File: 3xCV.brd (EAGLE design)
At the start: 96.8 x 54 mm, 90 parts, among them IC1 TL074, IC2 TL074, IC3 TL074, SW1 TL2285

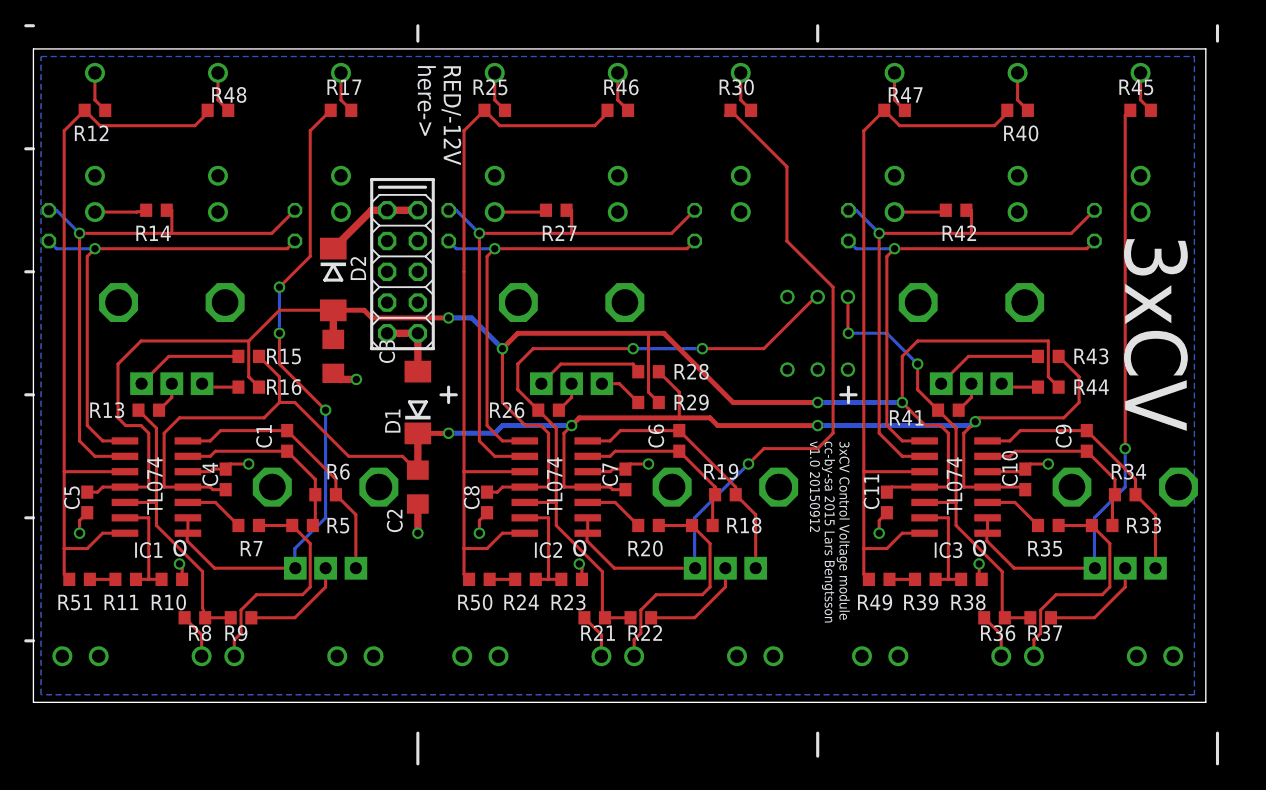
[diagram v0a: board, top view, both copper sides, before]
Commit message: Somewhat modified. No thru jacks (out of space). Aligned input jacks with outputs.
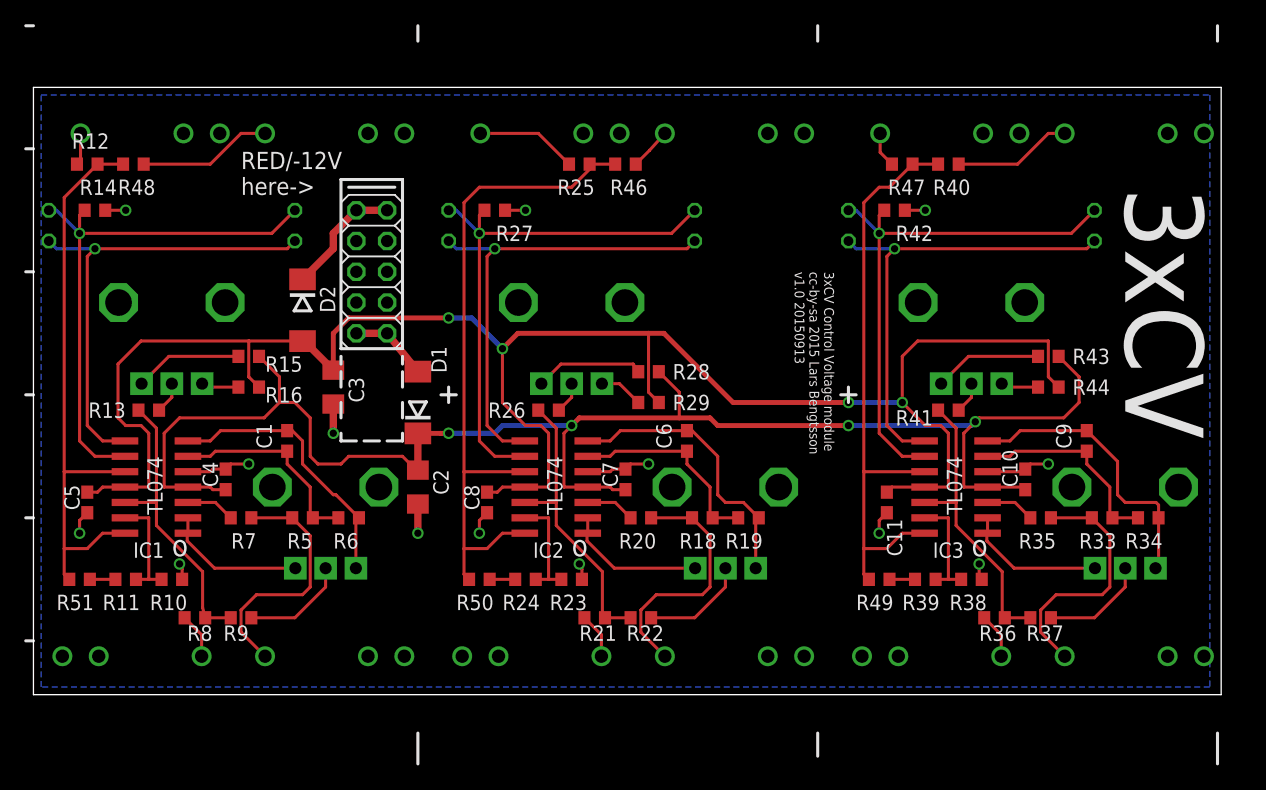
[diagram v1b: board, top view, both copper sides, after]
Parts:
- removed R17, R30, R45: 220, rcl:R0603
- removed SW1: TL2285, lb_devs:TL2285_PCB
- removed THRU, THRU1, THRU2: WQP-PJ301M-12_JACK, thonkiconn:WQP-PJ301M-12_JACK
- moved OUT2 8.89 mm to (91.4, 52.1), turned to 270 degrees
- moved OUT3 8.89 mm to (58.4, 52.1), turned to 270 degrees
- moved OUT5 8.89 mm to (25.4, 52.1), turned to 270 degrees
- moved R25 8.28 mm to (46.4, 49.5), turned to 180 degrees
- moved R48 8.28 mm to (9.53, 49.5)
- moved R40 7.24 mm to (76.8, 49.5)
- moved R27 5.08 mm to (39.4, 45.7), turned to 180 degrees
- moved R14 5.08 mm to (6.35, 45.7), turned to 180 degrees
- moved R42 5.08 mm to (72.4, 45.7), turned to 180 degrees
- moved R12 4.49 mm to (5.71, 49.5), turned to 180 degrees
- moved R47 4.49 mm to (73.0, 49.5), turned to 180 degrees
- moved R46 4.49 mm to (50.2, 49.5)
- moved OUT1 3.81 mm to (43.2, 52.1), turned to 270 degrees
- moved OUT4 3.81 mm to (76.2, 52.1), turned to 270 degrees
- moved OUT 3.81 mm to (10.2, 52.1), turned to 270 degrees
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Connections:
- removed net N$18: R17.2, THRU.P$1
- removed net N$38: R30.2, THRU1.P$1
- removed net N$55: R45.2, THRU2.P$1
- net GND: no longer THRU.P$3, THRU1.P$3, THRU2.P$3
- net MIX1: no longer SW1.3
- net MIX2: no longer SW1.2
- net N$25: no longer R30.1
- net N$42: no longer R45.1
- net N$5: no longer R17.1
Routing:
- net N$25: track 61.1 -> 11.8 mm, vias 1 -> 0
- net N$5: track 54.0 -> 11.8 mm, vias 3 -> 0
- net N$42: track 50.9 -> 11.8 mm, vias 1 -> 0
- net MIX2: track 55.7 -> 24.1 mm, vias 2 -> 0
- net MIX1: track 39.1 -> 24.8 mm, vias 2 -> 0
- net N$13: track 61.5 -> 48.3 mm
- net N$47: track 61.5 -> 49.3 mm
- net N$56: track 3.45 -> 11.1 mm
- net GND: track 43.5 -> 36.0 mm, vias 11 -> 14
- net N$49: track 3.45 -> 9.81 mm
- net N$57: track 61.5 -> 55.9 mm
- net N$32: track 3.45 -> 8.38 mm
- net N$55: track 3.45 -> 0.00 mm
- net N$38: track 3.45 -> 0.00 mm
- net N$18: track 3.45 -> 0.00 mm
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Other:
- board size 96.8 x 54 mm -> 98.1 x 50.2 mm
- board text added: "3xCV Control Voltage module cc-by-sa 2015 Lars Bengtsson v1.0 20150913"
- board text removed: "3xCV Control Voltage module cc-by-sa 2015 Lars Bengtsson v1.0 20150912"

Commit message: Added back 1+2 mix button. There is room for it. Yay! =)
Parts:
- added SW1: TL2285, lb_devs:TL2285_PCB
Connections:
- net MIX1: now also SW1.3
- net MIX2: now also SW1.2
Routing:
- net MIX1: track 24.8 -> 79.0 mm
- net MIX2: track 24.1 -> 73.9 mm
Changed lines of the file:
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@@
 <text x="45.72" y="17.145" size="1.778" layer="25" font="vector">o</text>
 <text x="78.74" y="17.145" size="1.778" layer="25" font="vector">o</text>
-<text x="64.135" y="40.64" size="0.8128" layer="25" font="vector" rot="SR270">3xCV Control Voltage module
+<text x="59.69" y="33.02" size="0.8128" layer="25" font="vector" rot="SR270">3xCV Control Voltage module
 cc-by-sa 2015 Lars Bengtsson
 v1.0 20150913</text>
@@
 <attribute name="VALUE" x="4.445" y="13.335" size="1.27" layer="27"/>
 </element>
+<element name="SW1" library="lb_devs" package="TL2285_PCB" value="TL2285" x="64.77" y="38.1" rot="MR0"/>
 </elements>
 <signals>
@@
 <wire x1="54.61" y1="28.575" x2="57.15" y2="28.575" width="0.4064" layer="1"/>
 <wire x1="57.15" y1="28.575" x2="57.785" y2="27.94" width="0.4064" layer="1"/>
-<wire x1="57.785" y1="27.94" x2="68.58" y2="27.94" width="0.4064" layer="1"/>
-<via x="68.58" y="27.94" extent="1-16" drill="0.6" shape="octagon"/>
-<wire x1="68.58" y1="27.94" x2="78.74" y2="27.94" width="0.4064" layer="16"/>
+<wire x1="57.785" y1="27.94" x2="66.04" y2="27.94" width="0.4064" layer="1"/>
+<via x="66.04" y="27.94" extent="1-16" drill="0.6" shape="octagon"/>
+<wire x1="66.04" y1="27.94" x2="78.74" y2="27.94" width="0.4064" layer="16"/>
 <wire x1="78.74" y1="27.94" x2="79.0575" y2="28.2575" width="0.4064" layer="16"/>
 <via x="79.0575" y="28.2575" extent="1-16" drill="0.6" shape="octagon"/>
@@
 <wire x1="52.07" y1="35.56" x2="53.34" y2="35.56" width="0.4064" layer="1"/>
 <wire x1="53.34" y1="35.56" x2="59.055" y2="29.845" width="0.4064" layer="1"/>
-<wire x1="59.055" y1="29.845" x2="68.58" y2="29.845" width="0.4064" layer="1"/>
-<via x="68.58" y="29.845" extent="1-16" drill="0.6" shape="octagon"/>
-<wire x1="68.58" y1="29.845" x2="73.025" y2="29.845" width="0.4064" layer="16"/>
+<wire x1="59.055" y1="29.845" x2="66.04" y2="29.845" width="0.4064" layer="1"/>
+<via x="66.04" y="29.845" extent="1-16" drill="0.6" shape="octagon"/>
+<wire x1="66.04" y1="29.845" x2="73.025" y2="29.845" width="0.4064" layer="16"/>
 <via x="73.025" y="29.845" extent="1-16" drill="0.6" shape="octagon"/>
 <wire x1="35.56" y1="36.83" x2="27.305" y2="36.83" width="0.4064" layer="1"/>
@@
 <wire x1="48.26" y1="15.875" x2="48.26" y2="12.28" width="0.254" layer="1"/>
 <wire x1="48.26" y1="12.28" x2="48.475" y2="12.065" width="0.254" layer="1"/>
-<wire x1="50.585" y1="12.065" x2="48.475" y2="12.065" width="0.254" layer="1"/>
+<wire x1="50.585" y1="12.065" x2="49.53" y2="12.065" width="0.254" layer="1"/>
+<contactref element="SW1" pad="2"/>
+<wire x1="49.53" y1="12.065" x2="48.475" y2="12.065" width="0.254" layer="1"/>
+<wire x1="67.31" y1="31.75" x2="67.31" y2="7.62" width="0.254" layer="1"/>
+<wire x1="67.31" y1="7.62" x2="66.675" y2="6.985" width="0.254" layer="1"/>
+<wire x1="66.675" y1="6.985" x2="52.705" y2="6.985" width="0.254" layer="1"/>
+<wire x1="52.705" y1="6.985" x2="49.53" y2="10.16" width="0.254" layer="1"/>
+<wire x1="49.53" y1="10.16" x2="49.53" y2="12.065" width="0.254" layer="1"/>
+<wire x1="67.31" y1="31.75" x2="64.77" y2="34.29" width="0.254" layer="1"/>
+<wire x1="64.77" y1="34.29" x2="64.77" y2="35.1" width="0.254" layer="1"/>
 </signal>
 <signal name="N$31">
@@
 <wire x1="77.47" y1="21.59" x2="77.47" y2="27.725" width="0.254" layer="1"/>
 <wire x1="77.47" y1="27.725" x2="75.985" y2="29.21" width="0.254" layer="1"/>
+<contactref element="SW1" pad="3"/>
+<wire x1="67.945" y1="32.385" x2="67.945" y2="7.62" width="0.254" layer="1"/>
+<wire x1="67.945" y1="7.62" x2="68.58" y2="6.985" width="0.254" layer="1"/>
+<wire x1="68.58" y1="6.985" x2="81.915" y2="6.985" width="0.254" layer="1"/>
+<wire x1="81.915" y1="6.985" x2="83.185" y2="8.255" width="0.254" layer="1"/>
+<wire x1="83.185" y1="8.255" x2="83.185" y2="11.645" width="0.254" layer="1"/>
+<wire x1="83.185" y1="11.645" x2="83.605" y2="12.065" width="0.254" layer="1"/>
+<wire x1="67.945" y1="32.385" x2="66.04" y2="34.29" width="0.254" layer="1"/>
+<wire x1="66.04" y1="34.29" x2="66.04" y2="36.195" width="0.254" layer="1"/>
+<wire x1="66.04" y1="36.195" x2="65.405" y2="36.83" width="0.254" layer="1"/>
+<wire x1="65.405" y1="36.83" x2="64" y2="36.83" width="0.254" layer="1"/>
+<wire x1="64" y1="36.83" x2="62.27" y2="35.1" width="0.254" layer="1"/>
 </signal>
 <signal name="N$47">
